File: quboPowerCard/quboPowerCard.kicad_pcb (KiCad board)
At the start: 2 copper layers, 14 parts, among them J4 Conn_01x04_Pin, J5 Conn_02x40_Odd_Even, J6 1720420202, Q1 IRF5305PbF, Q2 IRF5305PbF, U3 TSR2-2450, U4 TSR2-2433

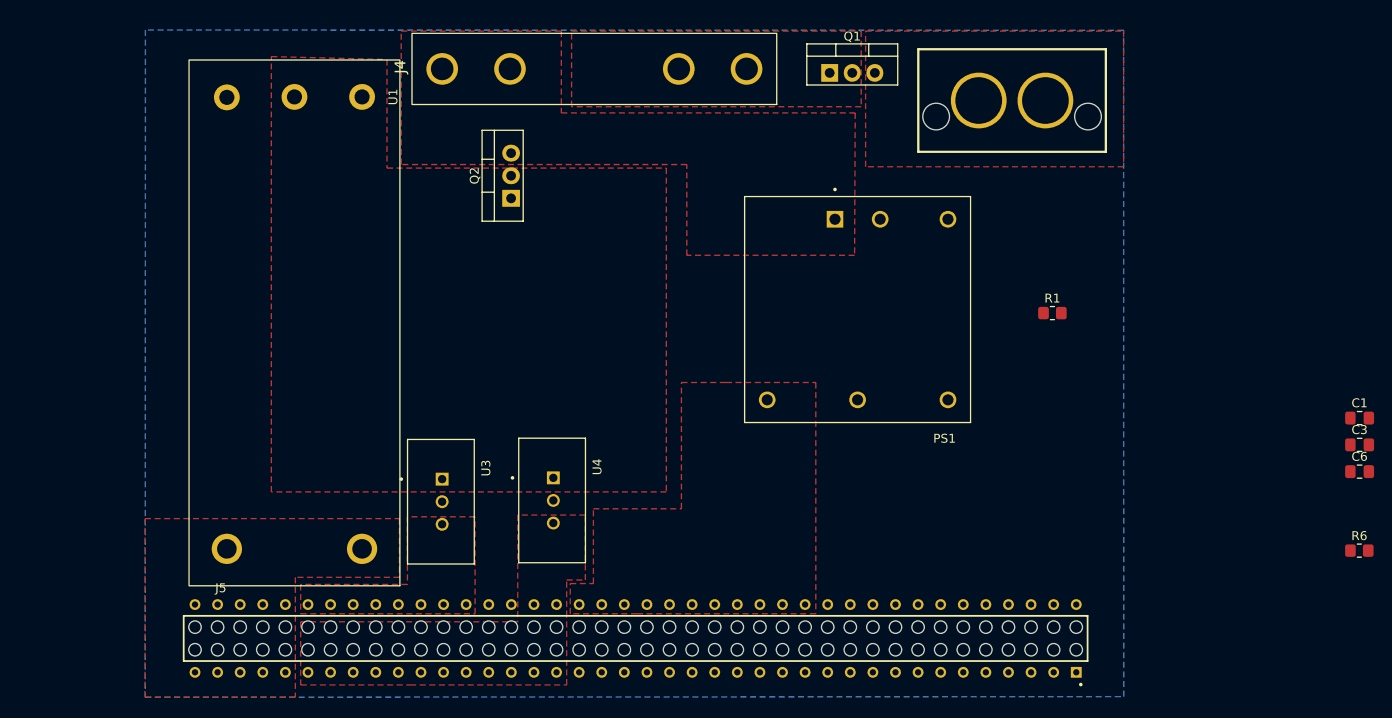
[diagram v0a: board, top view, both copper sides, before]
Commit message: power card update
put the resistors/capacitors in and added in the traces, also added the two switch jsts.
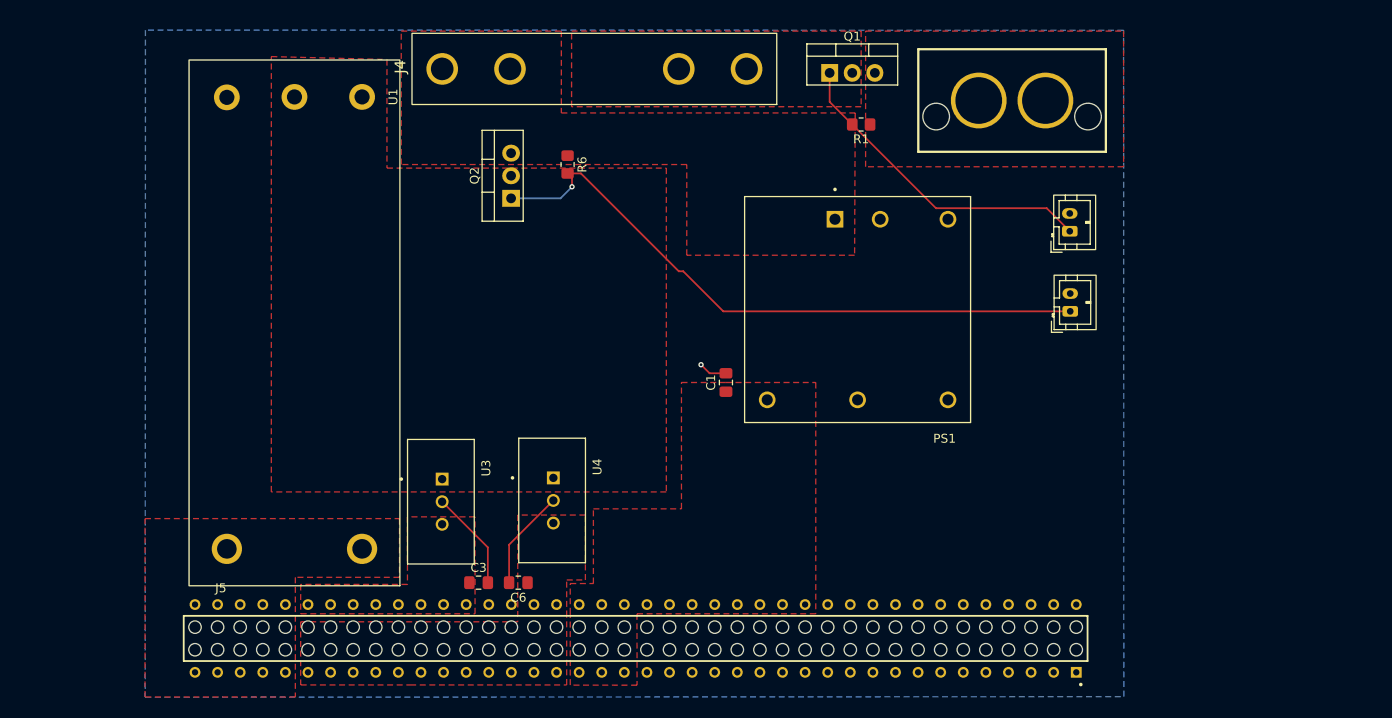
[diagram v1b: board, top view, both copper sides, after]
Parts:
- added J1: Conn_01x02_Pin, customRAM:JST_PH_B2B-PH-K_1x02_P2.00mm_Vertical, F.Cu at (224.0, 73.5)
- added J2: Conn_01x02_Pin, customRAM:JST_PH_B2B-PH-K_1x02_P2.00mm_Vertical, F.Cu at (223.9, 64.5)
- moved C3 100.2 mm to (157.5, 104.0)
- moved R6 99.0 mm to (167.5, 57.0), turned to -90 degrees
- moved C6 95.4 mm to (162.0, 104.0), turned to 180 degrees
- moved C1 71.3 mm to (185.3, 81.5), turned to 90 degrees
- moved R1 30.2 mm to (200.5, 52.5), turned to 180 degrees
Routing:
- net NPSW1: track 0.00 -> 72.0 mm, vias 0 -> 1
- net SW2: track 0.00 -> 36.3 mm
- net GND: track 0.00 -> 25.8 mm, vias 0 -> 1

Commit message: Changed Stackup to Pinheader
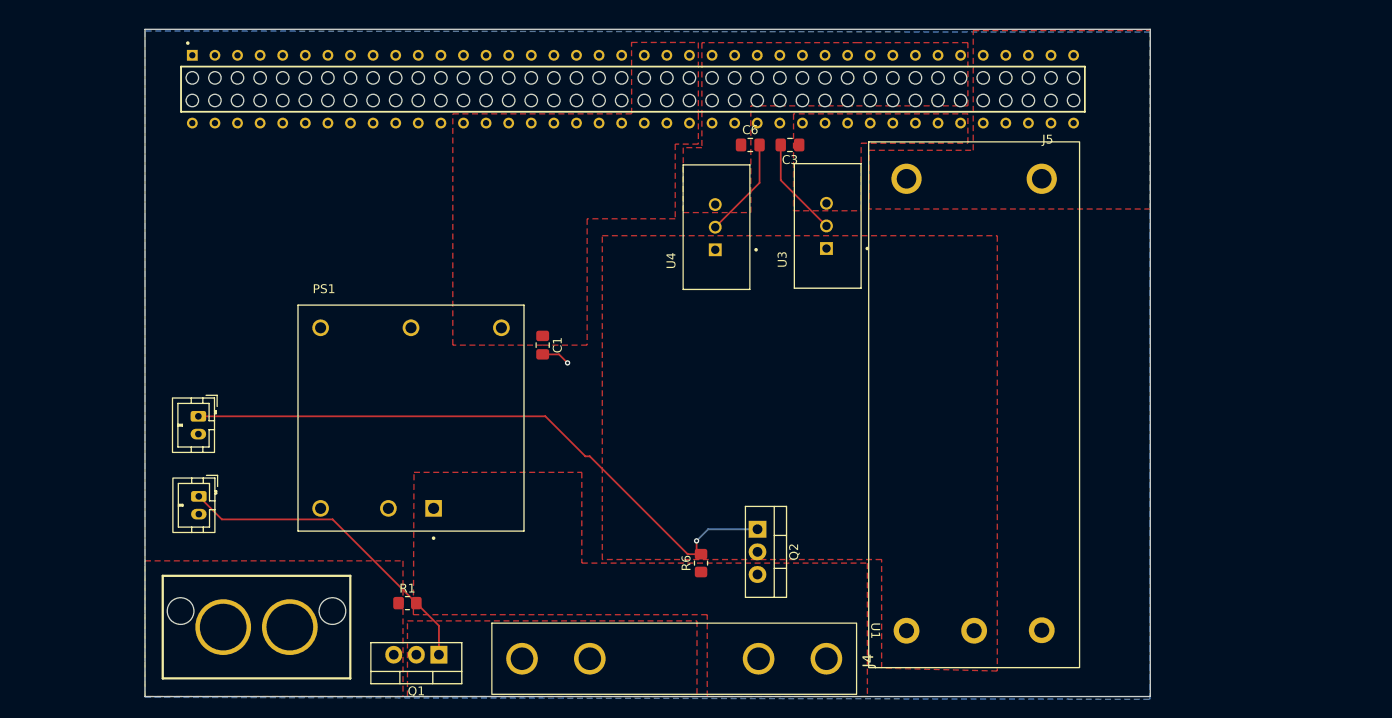
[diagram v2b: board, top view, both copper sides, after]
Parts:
- moved J6 103.5 mm to (132.5, 109.0), turned to 180 degrees
- moved J2 102.3 mm to (126.0, 94.3), turned to -90 degrees
- moved J1 98.7 mm to (126.0, 85.3), turned to -90 degrees
- moved U1 85.7 mm to (205.6, 109.4), turned to 0 degrees
- moved Q1 78.8 mm to (153.0, 112.1), turned to 180 degrees
- moved R1 74.1 mm to (149.5, 106.3), turned to 0 degrees
- moved J4 66.9 mm to (179.5, 112.5), turned to 0 degrees
- moved J5 61.7 mm to (174.8, 48.5), turned to 180 degrees
- moved C3 60.4 mm to (192.5, 54.8), turned to 180 degrees
- moved C6 55.7 mm to (188.0, 54.8), turned to 0 degrees
- moved U3 53.4 mm to (196.7, 63.9), turned to 90 degrees
- moved PS1 51.7 mm to (149.9, 85.5), turned to 0 degrees
- moved R6 47.2 mm to (182.5, 101.8), turned to 90 degrees
- moved Q2 46.4 mm to (188.8, 98.0), turned to -90 degrees
- moved U4 35.9 mm to (184.2, 64.0), turned to 90 degrees
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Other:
- board outline added: 113 x 75 mm
- board text added: "H5"

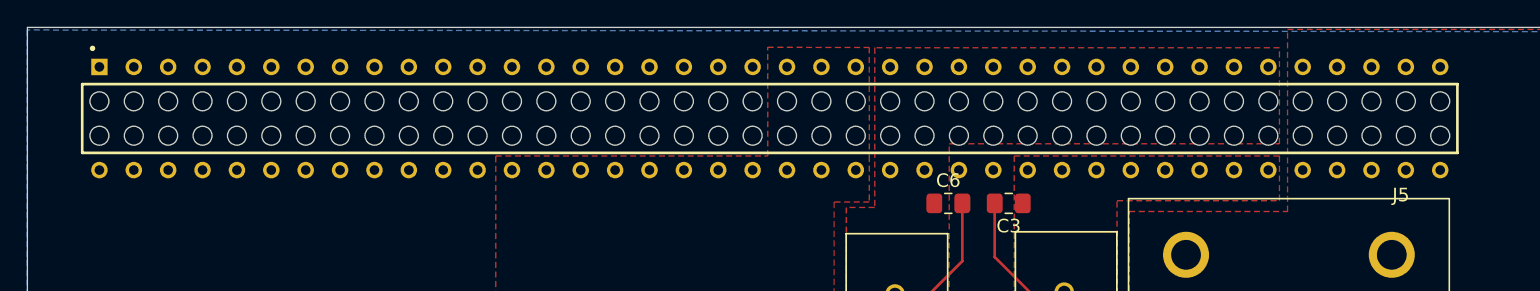
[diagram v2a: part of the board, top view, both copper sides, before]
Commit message: Changed connector orientation
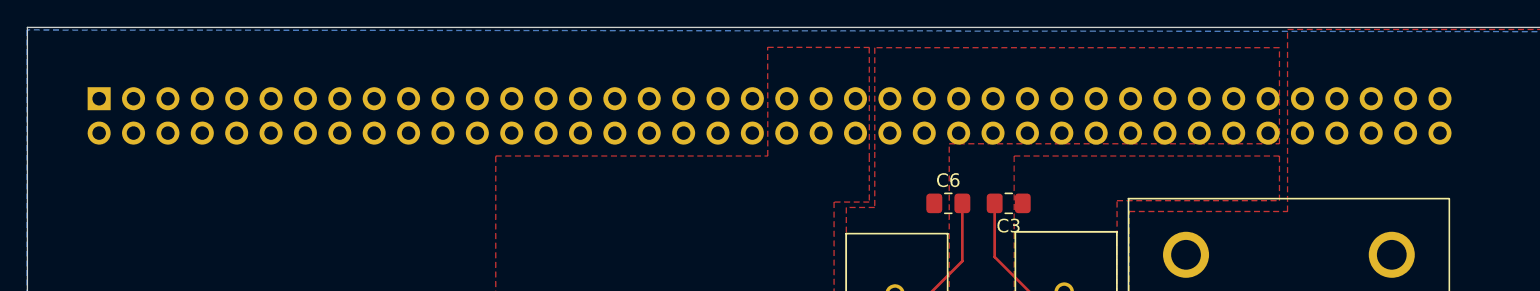
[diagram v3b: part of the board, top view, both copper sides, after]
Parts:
- J5: footprint customRAM:SAMTEC_HLE-140-02-L-DV-PE -> Connector_PinHeader_2.54mm:PinHeader_2x40_P2.54mm_Vertical; moved to B.Cu
- moved J5 49.6 mm to (125.3, 47.1), turned to -90 degrees

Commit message: Added Silkscreen, 12V Drops, Holes
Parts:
- added G***: LOGO, LOGO, F.Cu at (146.0, 59.3)
- added G***: LOGO, LOGO, B.Cu at (174.4, 83.2)
- added H1: MountingHole, MountingHole:MountingHole_2.2mm_M2, F.Cu at (120.4, 44.0)
- added H2: MountingHole, MountingHole:MountingHole_2.2mm_M2, F.Cu at (229.4, 44.0)
- added H3: MountingHole, MountingHole:MountingHole_2.2mm_M2, F.Cu at (229.4, 113.0)
- added J10: Conn_01x02_Pin, Connector_JST:JST_PH_B2B-PH-K_1x02_P2.00mm_Vertical, F.Cu at (228.9, 103.5)
- added J3: Conn_01x02_Pin, Connector_JST:JST_PH_B2B-PH-K_1x02_P2.00mm_Vertical, F.Cu at (229.0, 67.6)
- added J7: Conn_01x02_Pin, Connector_JST:JST_PH_B2B-PH-K_1x02_P2.00mm_Vertical, F.Cu at (229.0, 77.2)
- added J8: Conn_01x02_Pin, Connector_JST:JST_PH_B2B-PH-K_1x02_P2.00mm_Vertical, F.Cu at (228.9, 86.0)
- added J9: Conn_01x02_Pin, Connector_JST:JST_PH_B2B-PH-K_1x02_P2.00mm_Vertical, F.Cu at (228.9, 94.8)
- J1, J2: footprint customRAM:JST_PH_B2B-PH-K_1x02_P2.00mm_Vertical -> Connector_JST:JST_PH_B2B-PH-K_1x02_P2.00mm_Vertical
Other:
- board size 113 x 75 mm -> 116.3 x 76.3 mm
- board text added: "+12V"
- board text added: "All K/S"
- board text added: "Non-PI K/S"
- board text added: "Twobo Power 2026"
